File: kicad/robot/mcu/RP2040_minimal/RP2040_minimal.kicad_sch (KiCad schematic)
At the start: 37 parts, among them J2 Conn_02x07_Counter_Clockwise, Q5 SN74AHC125RGYR, U2 W25Q128JVS, U3 RP2040, Y1 ABLS-12.000MHZ-B4-T

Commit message: updated all footprint fields in schematic symbols with local robot ones
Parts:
- C10, C11, C12, C13, C14, C15, C16, C2, C3, C35, C36, C37, C38, C39, C5, C6, C7, C8, C9: footprint Capacitor_SMD:C_0402_1005Metric -> robot:C_0402_1005Metric
- C17: footprint Capacitor_SMD:C_0603_1608Metric -> robot:C_0603_1608Metric
- J2: footprint Connector_PinHeader_2.54mm:PinHeader_2x07_P2.54mm_Vertical -> robot:PinHeader_2x07_P2.54mm_Vertical
- Q5: footprint Ultra_Librarian:SN74AHC125RGYR -> robot:SN74AHC125RGYR
- R1, R2, R3, R4, R5: footprint Resistor_SMD:R_0402_1005Metric -> robot:R_0402_1005Metric
- R22, R23, R24, R25: footprint Resistor_SMD:R_0603_1608Metric -> robot:R_0603_1608Metric
- S2: footprint Button_Switch_SMD:TL3305AF160QG -> robot:TL3305AF160QG
- TP27: footprint Connector_PinHeader_2.54mm:PinHeader_1x02_P2.54mm_Vertical -> robot:PinHeader_1x02_P2.54mm_Vertical
- TP28: footprint TestPoint:TestPoint_2Pads_Pitch2mm_SMD -> robot:TestPoint_2Pads_Pitch2mm_SMD
- U2: footprint Package_SO:SOIC-8_5.23x5.23mm_P1.27mm -> robot:SOIC-8_5.23x5.23mm_P1.27mm
- U3: footprint RP2040_minimal:RP2040-QFN-56 -> robot:RP2040-QFN-56
- Y1: footprint RP2040_minimal:Crystal_SMD_HC49-US -> robot:Crystal_SMD_HC49-US

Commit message: Exported all schematic symbols to local robot and refer to them in all symbols
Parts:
- C10, C11, C12, C13, C14, C15, C16, C17, C2, C3, C35, C36, C37, C38, C39, C5, C6, C7, C8, C9: symbol Device:C -> robot:C
- J2: symbol Connector_Generic:Conn_02x07_Odd_Even -> robot:Conn_02x07_Odd_Even
- Q5: symbol ultralibrarian:SN74AHC125RGYR -> robot:SN74AHC125RGYR
- R1, R2, R22, R23, R24, R25, R3, R4, R5: symbol Device:R -> robot:R
- S2: symbol Switch:TL3305AF260QG -> robot:TL3305AF260QG
- TP27, TP28: symbol custom_connectors:TestPoint_CurrentShunt -> robot:TestPoint_CurrentShunt
- U2: symbol Memory_Flash:W25Q128JVS -> robot:W25Q128JVS
- U3: symbol MCU_RaspberryPi_RP2040:RP2040 -> robot:RP2040
- Y1: symbol Device:Crystal -> robot:Crystal
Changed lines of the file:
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@@
     (effects (font (size 1.27 1.27)) (justify right))
   )
-  (symbol (lib_id "MCU_RaspberryPi_RP2040:RP2040") (at 199.39 144.78 0) (unit 1)
+  (symbol (lib_id "robot:RP2040") (at 199.39 144.78 0) (unit 1)
     (in_bom yes) (on_board yes) (dnp no)
     (property "Reference" "U3" (at 171.45 95.25 0)
@@
     )
   )
-  (symbol (lib_id "Device:C") (at 52.07 218.44 270) (unit 1)
+  (symbol (lib_id "robot:C") (at 52.07 218.44 270) (unit 1)
     (in_bom yes) (on_board yes) (dnp no)
     (property "Reference" "C2" (at 50.8 211.8614 90)
@@
     )
   )
-  (symbol (lib_id "Device:C") (at 52.07 228.6 270) (unit 1)
+  (symbol (lib_id "robot:C") (at 52.07 228.6 270) (unit 1)
     (in_bom yes) (on_board yes) (dnp no)
     (property "Reference" "C3" (at 53.975 230.505 90)
@@
     )
   )
-  (symbol (lib_id "Memory_Flash:W25Q128JVS") (at 78.74 129.54 0) (unit 1)
+  (symbol (lib_id "robot:W25Q128JVS") (at 78.74 129.54 0) (unit 1)
     (in_bom yes) (on_board yes) (dnp no)
     (property "Reference" "U2" (at 69.85 119.38 0)
@@
     )
   )
-  (symbol (lib_id "Device:R") (at 63.5 110.49 0) (unit 1)
+  (symbol (lib_id "robot:R") (at 63.5 110.49 0) (unit 1)
     (in_bom no) (on_board yes) (dnp yes)
     (property "Reference" "R2" (at 65.278 109.3216 0)
@@
     )
   )
-  (symbol (lib_id "Device:R") (at 49.53 127 270) (unit 1)
+  (symbol (lib_id "robot:R") (at 49.53 127 270) (unit 1)
     (in_bom yes) (on_board yes) (dnp no)
     (property "Reference" "R1" (at 49.53 121.7422 90)
@@
     )
   )
-  (symbol (lib_id "Device:C") (at 86.36 107.95 0) (unit 1)
+  (symbol (lib_id "robot:C") (at 86.36 107.95 0) (unit 1)
     (in_bom yes) (on_board yes) (dnp no)
     (property "Reference" "C5" (at 89.281 106.7816 0)
@@
     )
   )
-  (symbol (lib_id "Device:R") (at 245.11 96.52 270) (unit 1)
+  (symbol (lib_id "robot:R") (at 245.11 96.52 270) (unit 1)
     (in_bom yes) (on_board yes) (dnp no)
     (property "Reference" "R3" (at 245.11 91.2622 90)
@@
     )
   )
-  (symbol (lib_id "Device:R") (at 245.11 104.14 270) (unit 1)
+  (symbol (lib_id "robot:R") (at 245.11 104.14 270) (unit 1)
     (in_bom yes) (on_board yes) (dnp no)
     (property "Reference" "R4" (at 245.11 98.8822 90)
@@
     )
   )
-  (symbol (lib_id "Device:C") (at 223.52 67.31 0) (unit 1)
+  (symbol (lib_id "robot:C") (at 223.52 67.31 0) (unit 1)
     (in_bom yes) (on_board yes) (dnp no)
     (property "Reference" "C9" (at 226.441 66.1416 0)
@@
     )
   )
-  (symbol (lib_id "Device:C") (at 236.22 67.31 0) (unit 1)
+  (symbol (lib_id "robot:C") (at 236.22 67.31 0) (unit 1)
     (in_bom yes) (on_board yes) (dnp no)
     (property "Reference" "C11" (at 239.141 66.1416 0)
@@
     )
   )
-  (symbol (lib_id "Device:C") (at 246.38 67.31 0) (unit 1)
+  (symbol (lib_id "robot:C") (at 246.38 67.31 0) (unit 1)
     (in_bom yes) (on_board yes) (dnp no)
     (property "Reference" "C12" (at 249.301 66.1416 0)
@@
     )
   )
-  (symbol (lib_id "Device:C") (at 259.08 67.31 0) (unit 1)
+  (symbol (lib_id "robot:C") (at 259.08 67.31 0) (unit 1)
     (in_bom yes) (on_board yes) (dnp no)
     (property "Reference" "C13" (at 262.001 66.1416 0)
@@
     )
   )
-  (symbol (lib_id "Device:C") (at 269.24 67.31 0) (unit 1)
+  (symbol (lib_id "robot:C") (at 269.24 67.31 0) (unit 1)
     (in_bom yes) (on_board yes) (dnp no)
     (property "Reference" "C14" (at 272.161 66.1416 0)
@@
     )
   )
-  (symbol (lib_id "Device:C") (at 281.94 67.31 0) (unit 1)
+  (symbol (lib_id "robot:C") (at 281.94 67.31 0) (unit 1)
     (in_bom yes) (on_board yes) (dnp no)
     (property "Reference" "C15" (at 284.861 66.1416 0)
@@
     )
   )
-  (symbol (lib_id "Device:C") (at 292.1 67.31 0) (unit 1)
+  (symbol (lib_id "robot:C") (at 292.1 67.31 0) (unit 1)
     (in_bom yes) (on_board yes) (dnp no)
     (property "Reference" "C16" (at 295.021 66.1416 0)
@@
     )
   )
-  (symbol (lib_id "Device:C") (at 157.48 67.31 0) (unit 1)
+  (symbol (lib_id "robot:C") (at 157.48 67.31 0) (unit 1)
     (in_bom yes) (on_board yes) (dnp no)
     (property "Reference" "C6" (at 160.655 64.77 0)
@@
     )
   )
-  (symbol (lib_id "Device:C") (at 170.18 67.31 0) (unit 1)
+  (symbol (lib_id "robot:C") (at 170.18 67.31 0) (unit 1)
     (in_bom yes) (on_board yes) (dnp no)
     (property "Reference" "C7" (at 173.355 64.9986 0)
@@
     )
   )
-  (symbol (lib_id "Device:C") (at 170.18 82.55 0) (unit 1)
+  (symbol (lib_id "robot:C") (at 170.18 82.55 0) (unit 1)
     (in_bom yes) (on_board yes) (dnp no)
     (property "Reference" "C8" (at 173.101 81.3816 0)
@@
     )
   )
-  (symbol (lib_id "Device:C") (at 223.52 82.55 0) (unit 1)
+  (symbol (lib_id "robot:C") (at 223.52 82.55 0) (unit 1)
     (in_bom yes) (on_board yes) (dnp no)
     (property "Reference" "C10" (at 226.441 81.3816 0)
@@
     )
   )
-  (symbol (lib_id "Device:R") (at 85.09 228.6 270) (unit 1)
+  (symbol (lib_id "robot:R") (at 85.09 228.6 270) (unit 1)
     (in_bom yes) (on_board yes) (dnp no)
     (property "Reference" "R5" (at 85.09 223.3422 90)
@@
     )
   )
-  (symbol (lib_id "Device:Crystal") (at 66.04 224.79 270) (unit 1)
+  (symbol (lib_id "robot:Crystal") (at 66.04 224.79 270) (unit 1)
     (in_bom yes) (on_board yes) (dnp no)
     (property "Reference" "Y1" (at 69.3674 223.6216 90)
@@
     )
   )
-  (symbol (lib_id "Device:C") (at 299.72 120.65 0) (unit 1)
+  (symbol (lib_id "robot:C") (at 299.72 120.65 0) (unit 1)
     (in_bom yes) (on_board yes) (dnp no)
     (property "Reference" "C17" (at 302.641 119.4816 0)
@@
     )
   )
-  (symbol (lib_id "Device:R") (at 304.8 264.16 270) (mirror x) (unit 1)
+  (symbol (lib_id "robot:R") (at 304.8 264.16 270) (mirror x) (unit 1)
     (in_bom yes) (on_board yes) (dnp no)
     (property "Reference" "R22" (at 307.34 260.35 90)
@@
     )
   )
-  (symbol (lib_id "ultralibrarian:SN74AHC125RGYR") (at 292.1 245.11 0) (unit 1)
+  (symbol (lib_id "robot:SN74AHC125RGYR") (at 292.1 245.11 0) (unit 1)
     (in_bom yes) (on_board yes) (dnp no)
     (property "Reference" "Q5" (at 297.18 227.33 0)
@@
     )
   )
-  (symbol (lib_id "Device:R") (at 347.98 233.68 270) (mirror x) (unit 1)
+  (symbol (lib_id "robot:R") (at 347.98 233.68 270) (mirror x) (unit 1)
     (in_bom yes) (on_board yes) (dnp no)
     (property "Reference" "R25" (at 350.52 229.87 90)
@@
     )
   )
-  (symbol (lib_id "Device:C") (at 336.55 267.97 0) (mirror y) (unit 1)
+  (symbol (lib_id "robot:C") (at 336.55 267.97 0) (mirror y) (unit 1)
     (in_bom yes) (on_board yes) (dnp no)
     (property "Reference" "C37" (at 340.36 266.6999 0)
@@
     )
   )
-  (symbol (lib_id "custom_connectors:TestPoint_CurrentShunt") (at 140.97 165.1 180) (unit 1)
+  (symbol (lib_id "robot:TestPoint_CurrentShunt") (at 140.97 165.1 180) (unit 1)
     (in_bom no) (on_board yes) (dnp no)
     (property "Reference" "TP28" (at 140.97 161.29 0)
@@
     )
   )
-  (symbol (lib_id "Device:C") (at 322.58 267.97 0) (mirror y) (unit 1)
+  (symbol (lib_id "robot:C") (at 322.58 267.97 0) (mirror y) (unit 1)
     (in_bom yes) (on_board yes) (dnp no)
     (property "Reference" "C36" (at 326.39 266.6999 0)
@@
     )
   )
-  (symbol (lib_id "Switch:TL3305AF260QG") (at 30.48 134.62 90) (unit 1)
+  (symbol (lib_id "robot:TL3305AF260QG") (at 30.48 134.62 90) (unit 1)
     (in_bom yes) (on_board yes) (dnp no)
     (property "Reference" "S2" (at 25.4 132.08 90)
@@
     )
   )
-  (symbol (lib_id "Device:C") (at 364.49 267.97 0) (mirror y) (unit 1)
+  (symbol (lib_id "robot:C") (at 364.49 267.97 0) (mirror y) (unit 1)
     (in_bom yes) (on_board yes) (dnp no)
     (property "Reference" "C39" (at 368.3 266.6999 0)
@@
     )
   )
-  (symbol (lib_id "Device:R") (at 334.01 243.84 270) (mirror x) (unit 1)
+  (symbol (lib_id "robot:R") (at 334.01 243.84 270) (mirror x) (unit 1)
     (in_bom yes) (on_board yes) (dnp no)
     (property "Reference" "R24" (at 336.55 240.03 90)
@@
     )
   )
-  (symbol (lib_id "custom_connectors:TestPoint_CurrentShunt") (at 143.51 177.8 90) (unit 1)
+  (symbol (lib_id "robot:TestPoint_CurrentShunt") (at 143.51 177.8 90) (unit 1)
     (in_bom yes) (on_board yes) (dnp no)
     (property "Reference" "TP27" (at 138.43 176.53 90)
@@
     )
   )
-  (symbol (lib_id "Device:C") (at 283.21 215.9 0) (unit 1)
+  (symbol (lib_id "robot:C") (at 283.21 215.9 0) (unit 1)
     (in_bom yes) (on_board yes) (dnp no)
     (property "Reference" "C35" (at 287.02 214.6299 0)
@@
     )
   )
-  (symbol (lib_id "Device:C") (at 350.52 267.97 0) (mirror y) (unit 1)
+  (symbol (lib_id "robot:C") (at 350.52 267.97 0) (mirror y) (unit 1)
     (in_bom yes) (on_board yes) (dnp no)
     (property "Reference" "C38" (at 354.33 266.6999 0)
@@
     )
   )
-  (symbol (lib_id "Connector_Generic:Conn_02x07_Odd_Even") (at 320.04 170.18 0) (unit 1)
+  (symbol (lib_id "robot:Conn_02x07_Odd_Even") (at 320.04 170.18 0) (unit 1)
     (in_bom yes) (on_board yes) (dnp no) (fields_autoplaced)
     (property "Reference" "J2" (at 321.31 157.71 0)
@@
     )
   )
-  (symbol (lib_id "Device:R") (at 320.04 254 270) (mirror x) (unit 1)
+  (symbol (lib_id "robot:R") (at 320.04 254 270) (mirror x) (unit 1)
     (in_bom yes) (on_board yes) (dnp no)
     (property "Reference" "R23" (at 322.58 250.19 90)

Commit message: Swapping out SW4_PTS815 SJM 250 SMTR LFS_CNK for prevvious tactile switch on rp2040
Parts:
- S2: value TL3305AF260QG -> PTS815 SJM 250 SMTR LFS; footprint robot:TL3305AF160QG -> robot:SW4_PTS815 SJM 250 SMTR LFS_CNK; Manufacturer (none) -> C&K; Manufacturer_Name E-Switch -> (none); Manufacturer_Part_Number TL3305AF260QG -> (none); Mouser Part Number 612-TL3305AF260QG -> (none); Mouser Price/Stock https://www.mouser.co.uk/ProductDetail/E-Switch/TL3305AF260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 -> (none); Part Number (none) -> PTS815 SJM 250 SMTR LFS
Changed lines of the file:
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@@
       (effects (font (size 1.27 1.27)) (justify right))
     )
-    (property "Value" "TL3305AF260QG" (at 36.322 123.436 90)
+    (property "Value" "PTS815 SJM 250 SMTR LFS" (at 36.322 123.436 90)
       (effects (font (size 1.27 1.27)) (justify right) hide)
     )
-    (property "Footprint" "robot:TL3305AF160QG" (at 125.4 118.11 0)
+    (property "Footprint" "robot:SW4_PTS815 SJM 250 SMTR LFS_CNK" (at 125.4 118.11 0)
       (effects (font (size 1.27 1.27)) (justify left top) hide)
     )
-    (property "Datasheet" "https://sten-eswitch-13110800-production.s3.amazonaws.com/system/asset/product_line/data_sheet/213/TL3305.pdf" (at 225.4 118.11 0)
+    (property "Datasheet" "" (at 225.4 118.11 0)
       (effects (font (size 1.27 1.27)) (justify left top) hide)
     )
-    (property "Height" "" (at 425.4 118.11 0)
-      (effects (font (size 1.27 1.27)) (justify left top) hide)
-    )
-    (property "Manufacturer_Name" "E-Switch" (at 525.4 118.11 0)
-      (effects (font (size 1.27 1.27)) (justify left top) hide)
-    )
-    (property "Manufacturer_Part_Number" "TL3305AF260QG" (at 625.4 118.11 0)
-      (effects (font (size 1.27 1.27)) (justify left top) hide)
-    )
-    (property "Mouser Part Number" "612-TL3305AF260QG" (at 725.4 118.11 0)
-      (effects (font (size 1.27 1.27)) (justify left top) hide)
-    )
-    (property "Mouser Price/Stock" "https://www.mouser.co.uk/ProductDetail/E-Switch/TL3305AF260QG?qs=UrFqKgNWc7QGfGfc5KSA7A%3D%3D" (at 825.4 118.11 0)
-      (effects (font (size 1.27 1.27)) (justify left top) hide)
-    )
-    (property "Arrow Part Number" "" (at 925.4 118.11 0)
-      (effects (font (size 1.27 1.27)) (justify left top) hide)
-    )
-    (property "Arrow Price/Stock" "" (at 1025.4 118.11 0)
-      (effects (font (size 1.27 1.27)) (justify left top) hide)
-    )
-    (property "Description" "" (at 30.48 134.62 0)
+    (property "Manufacturer" "C&K" (at 30.48 134.62 0)
       (effects (font (size 1.27 1.27)) hide)
     )
-    (property "Manufacturer" "" (at 30.48 134.62 0)
+    (property "Part Number" "PTS815 SJM 250 SMTR LFS" (at 30.48 134.62 0)
       (effects (font (size 1.27 1.27)) hide)
     )
-    (property "Manufacturer Part Number" "" (at 30.48 134.62 0)
-      (effects (font (size 1.27 1.27)) hide)
-    )
-    (property "Supplier" "" (at 30.48 134.62 0)
-      (effects (font (size 1.27 1.27)) hide)
-    )
-    (property "Supplier Part Number" "" (at 30.48 134.62 0)
-      (effects (font (size 1.27 1.27)) hide)
-    )
-    (property "Populated" "" (at 30.48 134.62 0)
-      (effects (font (size 1.27 1.27)) hide)
-    )
-    (property "ID" "" (at 30.48 134.62 0)
-      (effects (font (size 1.27 1.27)) hide)
-    )

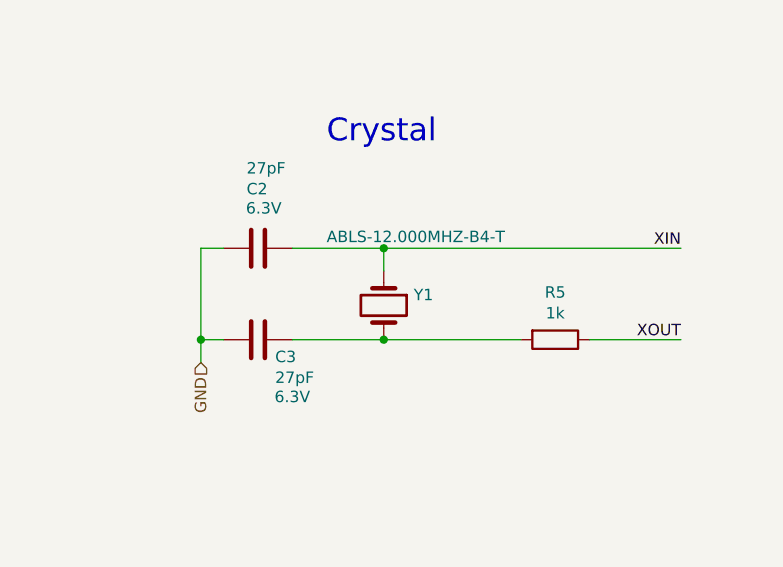
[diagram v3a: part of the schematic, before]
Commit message: Adding XTAL_ECS-120-8-36-CKM-TR3 in place of previous crystal
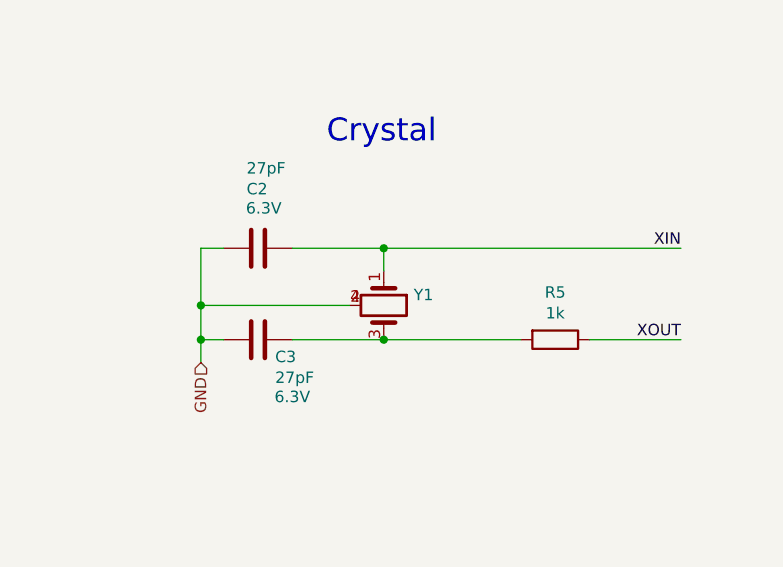
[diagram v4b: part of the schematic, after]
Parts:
- Y1: value ABLS-12.000MHZ-B4-T -> ECS-120-8-36-CKM-TR3; footprint robot:Crystal_SMD_HC49-US -> robot:XTAL_ECS-120-8-36-CKM-TR3; Manufacturer Abracon LLC -> ECS Inc.; Part Number ABLS-12.000MHZ-B4-T -> ECS-120-8-36-CKM-TR3
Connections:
- net GND: now also Y1.2 (GND), Y1.4 (GND)
- net at C3.1, R5.2: now also Y1.3; no longer Y1.2
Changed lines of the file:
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@@
   (junction (at 283.21 212.09) (diameter 0) (color 0 0 0 0)
+  )
+  (junction (at 45.72 224.79) (diameter 0) (color 0 0 0 0)
   )
   (junction (at 193.04 198.374) (diameter 0) (color 0 0 0 0)
@@
     (stroke (width 0) (type default))
   )
+  (wire (pts (xy 45.72 224.79) (xy 62.23 224.79))
+    (stroke (width 0) (type default))
+  )
   (wire (pts (xy 177.8 76.2) (xy 177.8 81.28))
     (stroke (width 0) (type default))
@@
     (stroke (width 0) (type default))
   )
+  (wire (pts (xy 45.72 224.79) (xy 45.72 228.6))
+    (stroke (width 0) (type default))
+  )
   (wire (pts (xy 48.26 228.6) (xy 45.72 228.6))
     (stroke (width 0) (type default))
@@
     (stroke (width 0) (type default))
   )
-  (wire (pts (xy 45.72 218.44) (xy 45.72 228.6))
+  (wire (pts (xy 45.72 218.44) (xy 45.72 224.79))
     (stroke (width 0) (type default))
   )
@@
       (effects (font (size 1.27 1.27)) (justify left))
     )
-    (property "Value" "ABLS-12.000MHZ-B4-T" (at 59.69 217.17 90)
-      (effects (font (size 1.27 1.27)) (justify left))
-    )
-    (property "Footprint" "robot:Crystal_SMD_HC49-US" (at 66.04 224.79 0)
-      (effects (font (size 1.27 1.27)) hide)
-    )
-    (property "Datasheet" "https://abracon.com/Resonators/ABLS.pdf" (at 66.04 224.79 0)
-      (effects (font (size 1.27 1.27)) hide)
-    )
-    (property "Manufacturer" "Abracon LLC" (at 66.04 224.79 0)
-      (effects (font (size 1.27 1.27)) hide)
-    )
-    (property "Part Number" "ABLS-12.000MHZ-B4-T" (at 66.04 224.79 0)
-      (effects (font (size 1.27 1.27)) hide)
-    )
-    (pin "1")
-    (pin "2")
-    (instances
-      (project "robot"
+    (property "Value" "ECS-120-8-36-CKM-TR3" (at 59.69 217.17 90)
+      (effects (font (size 1.27 1.27)) (justify left) hide)
+    )
+    (property "Footprint" "robot:XTAL_ECS-120-8-36-CKM-TR3" (at 66.04 224.79 0)
+      (effects (font (size 1.27 1.27)) hide)
+    )
+    (property "Datasheet" "https://ecsxtal.com/store/pdf/ECX-2236.pdf" (at 73.152 226.314 0)
+      (effects (font (size 1.27 1.27)) hide)
+    )
+    (property "Manufacturer" "ECS Inc." (at 73.152 224.79 0)
+      (effects (font (size 1.27 1.27)) hide)
+    )
+    (property "Part Number" "ECS-120-8-36-CKM-TR3" (at 72.644 225.806 0)
+      (effects (font (size 1.27 1.27)) hide)
+    )
+    (property "Description" "12 MHz ±10ppm Crystal 8pF 150 Ohms 4-SMD, No Lead" (at 72.898 224.79 0)
+      (effects (font (size 1.27 1.27)) hide)
+    )
+    (pin "1")
+    (pin "2")
+    (pin "3")
+    (pin "4")
+    (instances
+      (project "robot"

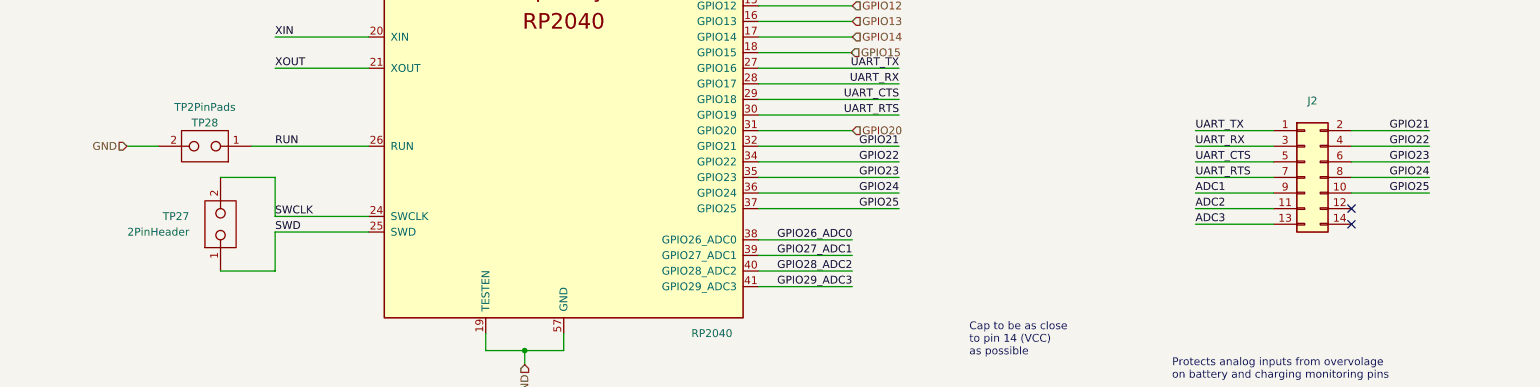
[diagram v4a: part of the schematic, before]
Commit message: Moving SWCLK and SWD to pin header on rp2040 UART
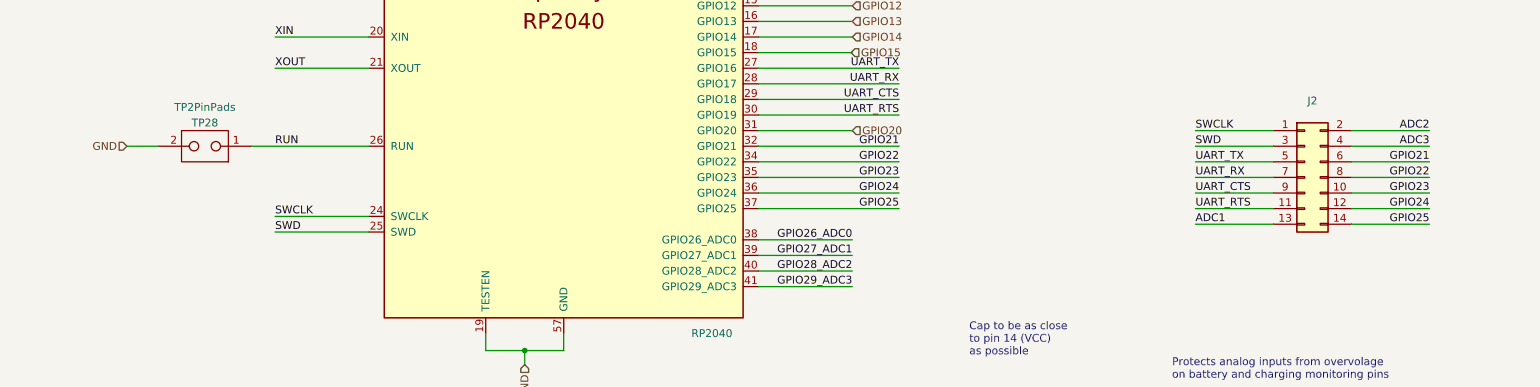
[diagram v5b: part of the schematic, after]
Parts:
- removed TP27: 2PinHeader, robot:PinHeader_1x02_P2.54mm_Vertical, symbol robot:TestPoint_CurrentShunt
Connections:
- net ADC1: now also J2.13 (Pin_13); no longer J2.9 (Pin_9)
- net ADC2: now also J2.2 (Pin_2); no longer J2.11 (Pin_11)
- net ADC3: now also J2.4 (Pin_4); no longer J2.13 (Pin_13)
- net GPIO21: now also J2.6 (Pin_6); no longer J2.2 (Pin_2)
- net GPIO22: now also J2.8 (Pin_8); no longer J2.4 (Pin_4)
- net GPIO23: now also J2.10 (Pin_10); no longer J2.6 (Pin_6)
- net GPIO24: now also J2.12 (Pin_12); no longer J2.8 (Pin_8)
- net GPIO25: now also J2.14 (Pin_14); no longer J2.10 (Pin_10)
- net SWCLK: now also J2.1 (Pin_1)
- net SWD: now also J2.3 (Pin_3)
- net UART_CTS: now also J2.9 (Pin_9); no longer J2.5 (Pin_5)
- net UART_RTS: now also J2.11 (Pin_11); no longer J2.7 (Pin_7)
- net UART_RX: now also J2.7 (Pin_7); no longer J2.3 (Pin_3)
- net UART_TX: now also J2.5 (Pin_5); no longer J2.1 (Pin_1)
- no-connect marks 2 -> 0
